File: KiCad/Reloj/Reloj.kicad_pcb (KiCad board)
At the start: 2 copper layers, 69.5 x 69.5 mm, 37 parts, among them J1 SOCKET_UP, J12 PLACA, J13 Conn_01x08_SocketMPU, J14 Conn_01x04_Socket, J15 Screw_Terminal_01x02, J16 Conn_01x02, J17 Conn_01x06_Socket, J18 Conn_01x02, J19 Conn_01x03, J21 Conn_01x02, J4 PLACA, J7 HEADER_DOWN, J8 PLACA, SW1 SW_SPDT, U1 25CSM04xxSN

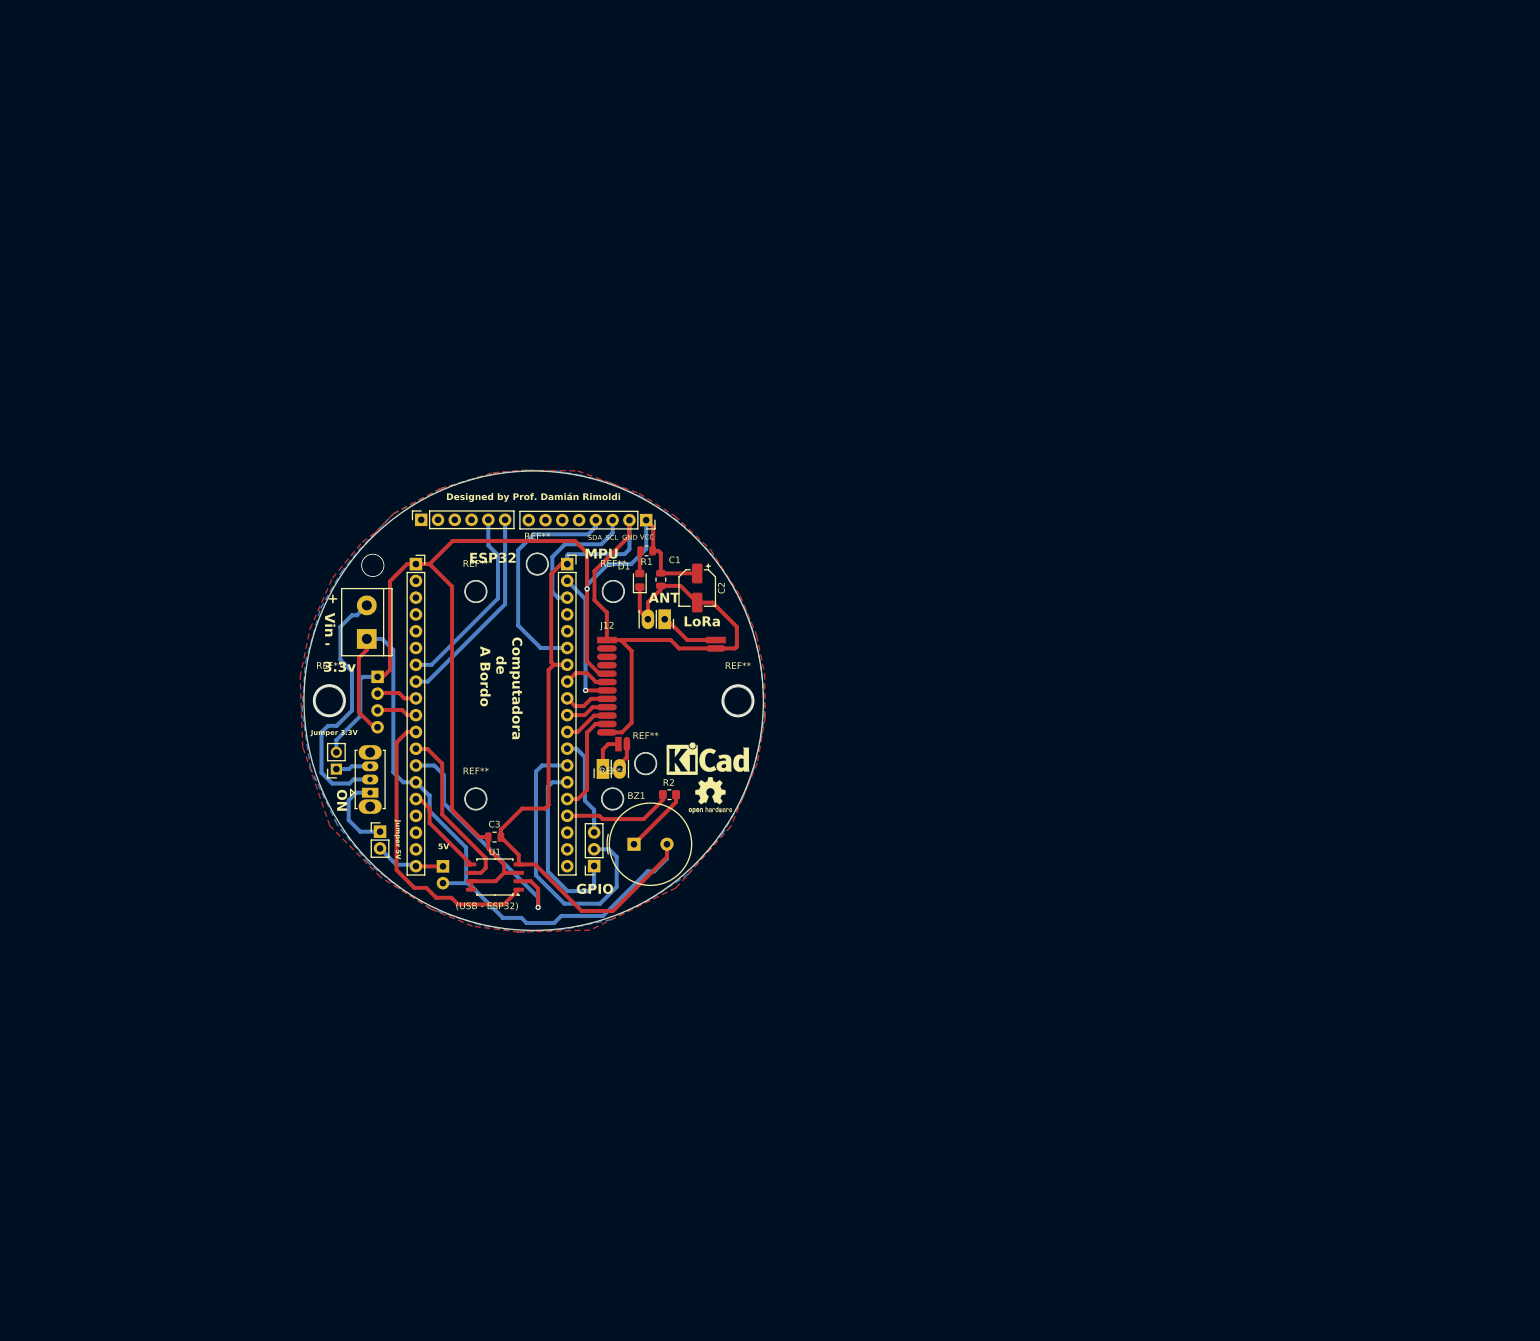
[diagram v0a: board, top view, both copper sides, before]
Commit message: Selecciono footprints y disposicion prelimar de PCB
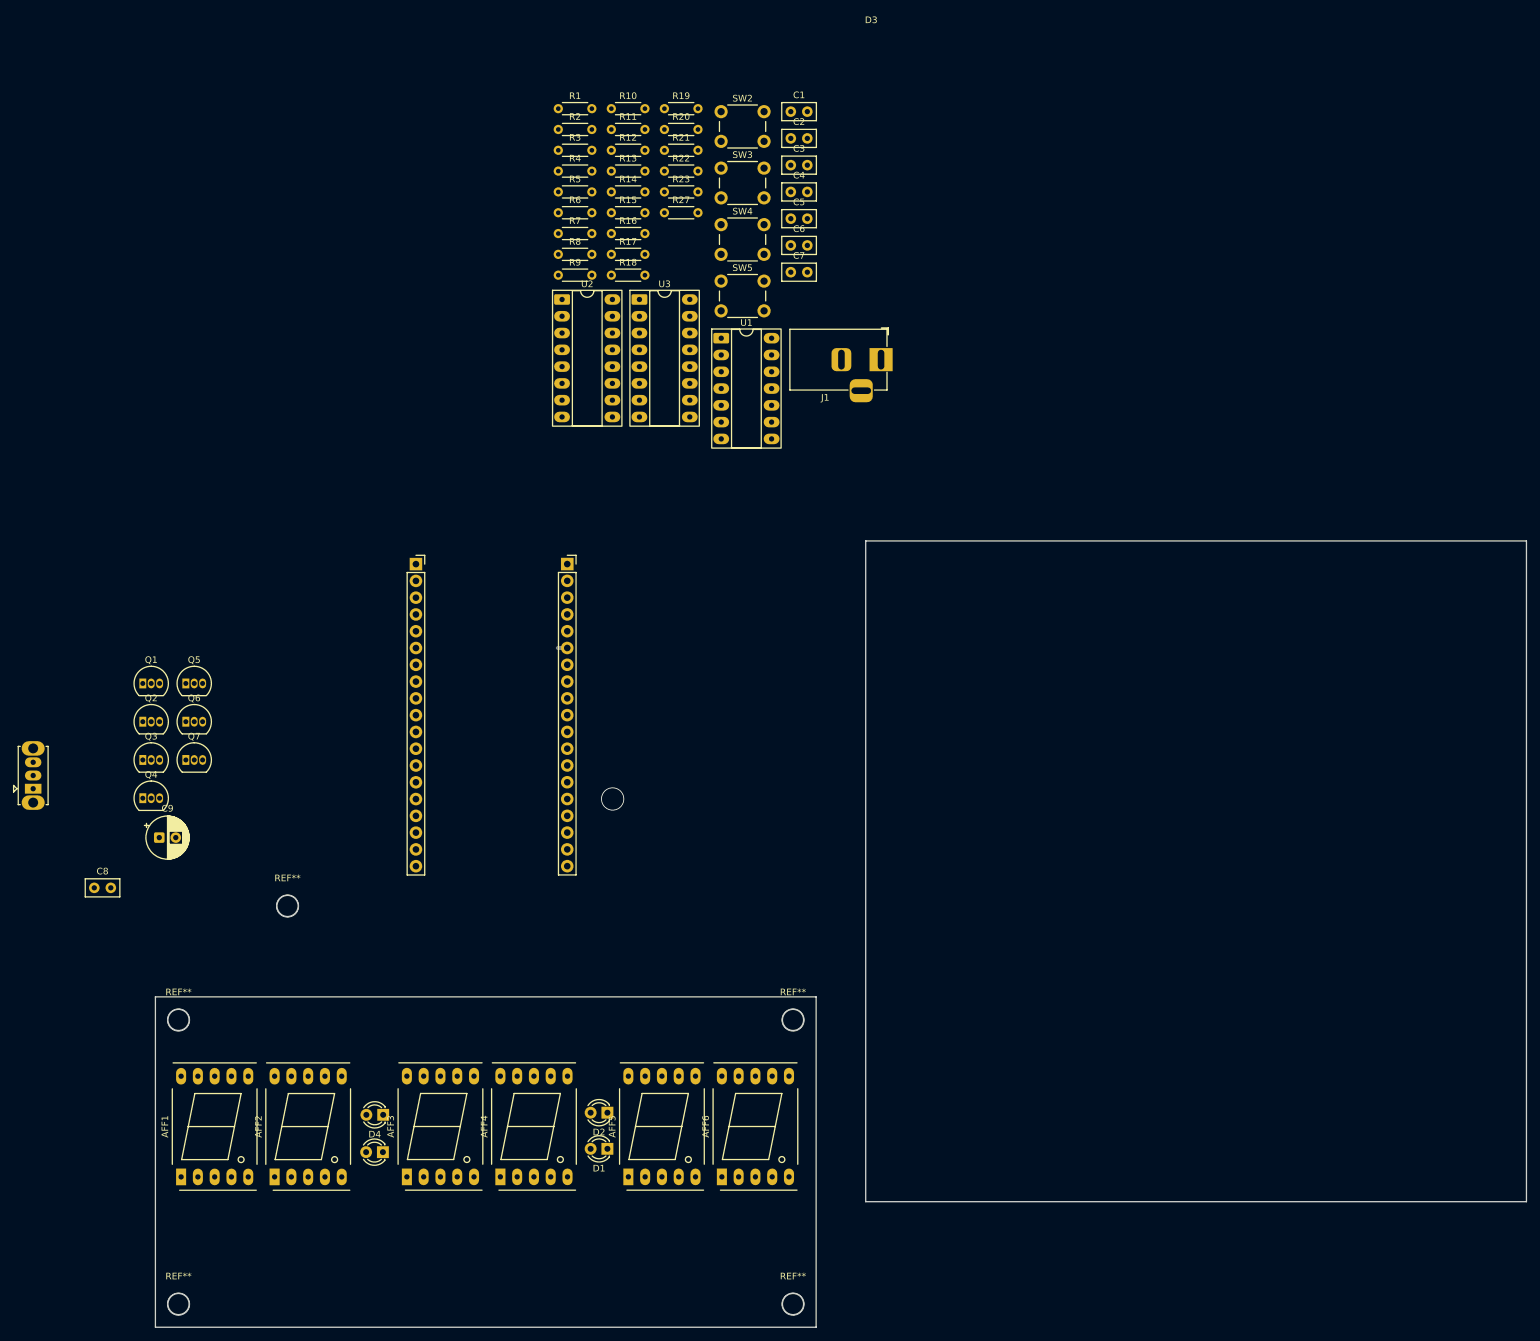
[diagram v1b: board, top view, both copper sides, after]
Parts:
- removed BZ1: Buzzer, Buzzer_Beeper:Buzzer_TDK_PS1240P02BT_D12.2mm_H6.5mm
- removed G***: LOGO, Imagenes:Cohete2
- removed G***: LOGO, Imagenes:CDRSys2Chico
- removed J12: PLACA, Connector_PinHeader_1.27mm:PinHeader_1x12_P1.27mm_Vertical
- removed J13: Conn_01x08_SocketMPU, Connector_PinSocket_2.54mm:PinSocket_1x08_P2.54mm_Vertical
- removed J14: Conn_01x04_Socket, Connector_PinSocket_2.54mm:PinSocket_1x04_P2.54mm_Vertical
- removed J15: Screw_Terminal_01x02, TerminalBlock:TerminalBlock_bornier-2_P5.08mm
- removed J16, J21: Conn_01x02, Connector_PinSocket_2.54mm:PinSocket_1x02_P2.54mm_Vertical
- removed J17: Conn_01x06_Socket, Connector_PinSocket_2.54mm:PinSocket_1x06_P2.54mm_Vertical
- removed J18: Conn_01x02, Connector_PinHeader_2.54mm:PinHeader_1x02_P2.54mm_Vertical
- removed J19: Conn_01x03, Connector_PinSocket_2.54mm:PinSocket_1x03_P2.54mm_Vertical
- removed J4, J8: PLACA, Connector_PinHeader_1.27mm:PinHeader_1x02_P1.27mm_Vertical
- removed J7: HEADER_DOWN, Connector_PinHeader_2.54mm:PinHeader_1x02_P2.54mm_Vertical
- removed the REF** at (112.2, 55.7)
- removed the REF** at (108.0, 70.0)
- removed the REF** at (104.3, 69.9)
- removed the REF** at (72.5, 39.1)
- removed the REF** at (107.6, 65.0)
- removed the REF** at (81.8, 35.0)
- removed the REF** at (98.2, 65.2)
- removed the REF** at (50.3, 55.7)
- removed the REF** at (93.3, 39.1)
- removed the REF** at (93.2, 70.5)
- added AFF1: LTS-6980HR, Display_7Segment:7SegmentLED_LTS6760_LTS6780, F.Cu at (27.9, 127.8)
- added AFF2: LTS-6980HR, Display_7Segment:7SegmentLED_LTS6760_LTS6780, F.Cu at (42.0, 127.8)
- added AFF3: LTS-6980HR, Display_7Segment:7SegmentLED_LTS6760_LTS6780, F.Cu at (62.1, 127.7)
- added AFF4: LTS-6980HR, Display_7Segment:7SegmentLED_LTS6760_LTS6780, F.Cu at (76.2, 127.7)
- added AFF5: LTS-6980HR, Display_7Segment:7SegmentLED_LTS6760_LTS6780, F.Cu at (95.6, 127.7)
- added AFF6: LTS-6980HR, Display_7Segment:7SegmentLED_LTS6760_LTS6780, F.Cu at (109.7, 127.7)
- added C4: 0.1uF, Capacitor_THT:C_Disc_D5.0mm_W2.5mm_P2.50mm, F.Cu at (120.2, -21.3)
- added C5: 0.1uF, Capacitor_THT:C_Disc_D5.0mm_W2.5mm_P2.50mm, F.Cu at (120.2, -17.3)
- added C6: 0.1uF, Capacitor_THT:C_Disc_D5.0mm_W2.5mm_P2.50mm, F.Cu at (120.2, -13.2)
- added C7: 0.1uF, Capacitor_THT:C_Disc_D5.0mm_W2.5mm_P2.50mm, F.Cu at (120.2, -9.18)
- added C8: 0.1uF, Capacitor_THT:C_Disc_D5.0mm_W2.5mm_P2.50mm, F.Cu at (14.8, 84.0)
- added C9: 100uF 16V, Capacitor_THT:CP_Radial_D6.3mm_P2.50mm, F.Cu at (24.6, 76.4)
- added D2: LED, LED_THT:LED_D3.0mm, F.Cu at (92.4, 118.0)
- added D3: LED, LED_THT:LED_D3.0mm, F.Cu at (58.4, 124.0)
- added D4: LED, LED_THT:LED_D3.0mm, F.Cu at (58.5, 118.4)
- added Q1: BC548, Package_TO_SOT_THT:TO-92_Inline, F.Cu at (22.1, 53.1)
- added Q2: BC548, Package_TO_SOT_THT:TO-92_Inline, F.Cu at (22.1, 58.9)
- added Q3: BC548, Package_TO_SOT_THT:TO-92_Inline, F.Cu at (22.1, 64.6)
- added Q4: BC548, Package_TO_SOT_THT:TO-92_Inline, F.Cu at (22.1, 70.4)
- added Q5: BC548, Package_TO_SOT_THT:TO-92_Inline, F.Cu at (28.6, 53.1)
- added Q6: BC548, Package_TO_SOT_THT:TO-92_Inline, F.Cu at (28.6, 58.9)
- added Q7: BC548, Package_TO_SOT_THT:TO-92_Inline, F.Cu at (28.6, 64.6)
- added R10: 4.7k, Resistor_THT:R_Axial_DIN0204_L3.6mm_D1.6mm_P5.08mm_Horizontal, F.Cu at (93.0, -33.9)
- added R11: 4.7k, Resistor_THT:R_Axial_DIN0204_L3.6mm_D1.6mm_P5.08mm_Horizontal, F.Cu at (93.0, -30.8)
- added R12: 4.7k, Resistor_THT:R_Axial_DIN0204_L3.6mm_D1.6mm_P5.08mm_Horizontal, F.Cu at (93.0, -27.6)
- added R13: 4.7k, Resistor_THT:R_Axial_DIN0204_L3.6mm_D1.6mm_P5.08mm_Horizontal, F.Cu at (93.0, -24.5)
- added R14: 4.7k, Resistor_THT:R_Axial_DIN0204_L3.6mm_D1.6mm_P5.08mm_Horizontal, F.Cu at (93.0, -21.3)
- added R15: 100, Resistor_THT:R_Axial_DIN0204_L3.6mm_D1.6mm_P5.08mm_Horizontal, F.Cu at (93.0, -18.2)
- added R16: 100, Resistor_THT:R_Axial_DIN0204_L3.6mm_D1.6mm_P5.08mm_Horizontal, F.Cu at (93.0, -15.0)
- added R17: 330, Resistor_THT:R_Axial_DIN0204_L3.6mm_D1.6mm_P5.08mm_Horizontal, F.Cu at (93.0, -11.9)
- added R18: 330, Resistor_THT:R_Axial_DIN0204_L3.6mm_D1.6mm_P5.08mm_Horizontal, F.Cu at (93.0, -8.72)
- added R19: 330, Resistor_THT:R_Axial_DIN0204_L3.6mm_D1.6mm_P5.08mm_Horizontal, F.Cu at (101.0, -33.9)
- added R20: 330, Resistor_THT:R_Axial_DIN0204_L3.6mm_D1.6mm_P5.08mm_Horizontal, F.Cu at (101.0, -30.8)
- added R21: 330, Resistor_THT:R_Axial_DIN0204_L3.6mm_D1.6mm_P5.08mm_Horizontal, F.Cu at (101.0, -27.6)
- added R22: 330, Resistor_THT:R_Axial_DIN0204_L3.6mm_D1.6mm_P5.08mm_Horizontal, F.Cu at (101.0, -24.5)
- added R23: 330, Resistor_THT:R_Axial_DIN0204_L3.6mm_D1.6mm_P5.08mm_Horizontal, F.Cu at (101.0, -21.3)
- added R27: 4.7k, Resistor_THT:R_Axial_DIN0204_L3.6mm_D1.6mm_P5.08mm_Horizontal, F.Cu at (101.0, -18.2)
- added R3: 10K, Resistor_THT:R_Axial_DIN0204_L3.6mm_D1.6mm_P5.08mm_Horizontal, F.Cu at (85.0, -27.6)
- added R4: 100, Resistor_THT:R_Axial_DIN0204_L3.6mm_D1.6mm_P5.08mm_Horizontal, F.Cu at (85.0, -24.5)
- added R5: 10K, Resistor_THT:R_Axial_DIN0204_L3.6mm_D1.6mm_P5.08mm_Horizontal, F.Cu at (85.0, -21.3)
- added R6: 100, Resistor_THT:R_Axial_DIN0204_L3.6mm_D1.6mm_P5.08mm_Horizontal, F.Cu at (85.0, -18.2)
- added R7: 10K, Resistor_THT:R_Axial_DIN0204_L3.6mm_D1.6mm_P5.08mm_Horizontal, F.Cu at (85.0, -15.0)
- added R8: 100, Resistor_THT:R_Axial_DIN0204_L3.6mm_D1.6mm_P5.08mm_Horizontal, F.Cu at (85.0, -11.9)
- added R9: 4.7k, Resistor_THT:R_Axial_DIN0204_L3.6mm_D1.6mm_P5.08mm_Horizontal, F.Cu at (85.0, -8.72)
- added REF**: MountingHole_3.2mm_M3, MountingHole:MountingHole_3.2mm_M3, F.Cu at (27.5, 147.0)
- added REF**: MountingHole_3.2mm_M3, MountingHole:MountingHole_3.2mm_M3, F.Cu at (120.5, 147.0)
- added REF**: MountingHole_3.2mm_M3, MountingHole:MountingHole_3.2mm_M3, F.Cu at (27.5, 104.0)
- added REF**: MountingHole_3.2mm_M3, MountingHole:MountingHole_3.2mm_M3, F.Cu at (120.5, 104.0)
- added SW2: SW_Push, Button_Switch_THT:SW_PUSH_6mm_H4.3mm, F.Cu at (109.6, -33.5)
- added SW3: SW_Push, Button_Switch_THT:SW_PUSH_6mm_H4.3mm, F.Cu at (109.6, -24.9)
- added SW4: SW_Push, Button_Switch_THT:SW_PUSH_6mm_H4.3mm, F.Cu at (109.6, -16.4)
- added SW5: SW_Push, Button_Switch_THT:SW_PUSH_6mm_H4.3mm, F.Cu at (109.6, -7.83)
- added U2: 4050, Package_DIP:DIP-16_W7.62mm_Socket_LongPads, F.Cu at (85.5, -5.04)
- added U3: 74HC595, Package_DIP:DIP-16_W7.62mm_Socket_LongPads, F.Cu at (97.3, -5.04)
- C1: value 100nF -> 0.1uF; footprint Capacitor_SMD:C_0805_2012Metric -> Capacitor_THT:C_Disc_D5.0mm_W2.5mm_P2.50mm
- C2: value 100uF -> 0.1uF; footprint Capacitor_SMD:CP_Elec_5x3.9 -> Capacitor_THT:C_Disc_D5.0mm_W2.5mm_P2.50mm
- C3: value C_Polarized_Small -> 0.1uF; footprint Capacitor_SMD:C_0805_2012Metric -> Capacitor_THT:C_Disc_D5.0mm_W2.5mm_P2.50mm
- D1: footprint LED_SMD:LED_0805_2012Metric_Pad1.15x1.40mm_HandSolder -> LED_THT:LED_D3.0mm
- J1: value SOCKET_UP -> Jack-DC; footprint Connector_PinSocket_2.54mm:PinSocket_1x02_P2.54mm_Vertical -> Connector_BarrelJack:BarrelJack_Horizontal
- R1: value 1K -> 10K; footprint Resistor_SMD:R_0805_2012Metric -> Resistor_THT:R_Axial_DIN0204_L3.6mm_D1.6mm_P5.08mm_Horizontal
- R2: value R -> 100; footprint Resistor_SMD:R_0805_2012Metric_Pad1.20x1.40mm_HandSolder -> Resistor_THT:R_Axial_DIN0204_L3.6mm_D1.6mm_P5.08mm_Horizontal
- U1: value 25CSM04xxSN -> 74HC14; footprint Package_SO:SOIC-8_5.23x5.23mm_P1.27mm -> Package_DIP:DIP-14_W7.62mm_Socket_LongPads
- moved C3 111.1 mm to (120.2, -25.4)
- moved R2 102.1 mm to (85.0, -30.8), turned to 0 degrees
- moved U1 88.5 mm to (109.6, 0.81), turned to 0 degrees
- moved D1 86.2 mm to (92.4, 123.5), turned to 180 degrees
- moved C1 73.5 mm to (120.2, -33.5), turned to 0 degrees
- moved C2 69.5 mm to (120.2, -29.4), turned to 0 degrees
- moved R1 68.3 mm to (85.0, -33.9), turned to 0 degrees
- moved J1 51.1 mm to (133.8, 4.06), turned to 0 degrees
- moved SW1 51.0 mm to (5.50, 69.0)
- moved REF** 32.8 mm to (44.0, 86.7)
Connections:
- C1 pad 1: VCC -> Net-(C1-Pad1)
- C2 pad 1: VCC -> Net-(C2-Pad1)
- C3 pad 1: VCC -> Net-(C3-Pad1)
- D1 pad 1: GND -> Net-(D1-K)
- D1 pad 2: Net-(D1-A) -> 3,3V
- J1 pad 1: ANTENA -> GND
- J1 pad 2: GND -> 5v
- R1 pad 1: VCC -> 3,3V
- R1 pad 2: Net-(D1-A) -> Net-(R1-Pad2)
- R2 pad 1: Net-(BZ1-+) -> Net-(C1-Pad1)
- R2 pad 2: BUZZ -> Net-(R1-Pad2)
- U1 pad 1: HSS -> Net-(C1-Pad1)
- U1 pad 2: HMISO -> GPIO32
- U1 pad 3: VCC -> Net-(C2-Pad1)
- U1 pad 4: GND -> GPIO33
- U1 pad 5: HMOSI -> Net-(C3-Pad1)
- U1 pad 6: HCLK -> GPIO25
- U1 pad 7: VCC -> Net-(U1G-GND)
- U1 pad 8: VCC -> GPIO26
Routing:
- net GND: track 297.0 -> 0.17 mm
- net VCC: track 178.0 -> 0.00 mm, vias 1 -> 0
- net HSS: track 44.5 -> 0.00 mm
- net GPIO4: track 44.3 -> 0.00 mm
- net INVolt: track 39.1 -> 0.00 mm
- net HMISO: track 37.1 -> 0.02 mm, vias 1 -> 0
- net SDAMPU: track 35.6 -> 1.43 mm
- net GPIO33: track 31.1 -> 0.00 mm
- net GPIO32: track 29.1 -> 0.00 mm
- net GPIO0: track 27.7 -> 0.21 mm
- net HCLK: track 26.0 -> 0.08 mm
- net MOSI: track 21.0 -> 0.00 mm, vias 1 -> 0
- net SCLMPU: track 20.5 -> 0.00 mm
- net BUZZ: track 16.7 -> 0.00 mm
- net REST: track 15.8 -> 0.00 mm
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- removed copper zone on B.Cu, net GND
- removed copper zone on F.Cu, net GND
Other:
- board size 69.5 x 69.5 mm -> 207.5 x 119 mm
- board text removed: "(USB - ESP32)"
- board text removed: "+"
- board text removed: "-"
- board text removed: "3.3v"
- board text removed: "5V"
- board text removed: "ANT"
- board text removed: "CANSAT 2024"
- board text removed: "Computadora de A Bordo"
- board text removed: "Designed by Prof. Damián Rimoldi"
- board text removed: "ESP32"
- board text removed: "GND"
- board text removed: "GPIO"
- board text removed: "GPS"
- board text removed: "Jumper 3.3V"
- board text removed: "Jumper 5V"
- board text removed: "LoRa"
- board text removed: "MPU"
- board text removed: "ON"
- board text removed: "P0"
- board text removed: "P16"
- board text removed: "P32"
- board text removed: "P33"
- board text removed: "P34"
- board text removed: "P35"
- board text removed: "P36"
- board text removed: "P39"
- board text removed: "P4"
- board text removed: "Rev 1.0.0"
- board text removed: "Rx"
- board text removed: "SAGA I"
- board text removed: "SCL"
- board text removed: "SDA"
- board text removed: "Tx"
- board text removed: "UTN - EESTNº4"
- board text removed: "VCC"
- board text removed: "Vin"
- board text removed: "_"

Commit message: Agrego version 3 placas, distribucion principal y conectores
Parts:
- removed the REF** at (44.0, 86.7)
- added J2: Conn_2Rows-15Pins, Connector_IDC:IDC-Header_2x07_P2.54mm_Vertical, F.Cu at (95.8, 146.5)
- added J3: Conn_2Rows-11Pins, Connector_IDC:IDC-Header_2x05_P2.54mm_Vertical, F.Cu at (36.8, 146.5)
- added J4: Conn_2Rows-15Pins, Connector_IDC:IDC-Header_2x07_P2.54mm_Vertical, F.Cu at (213.9, 145.5)
- added J5: Conn_2Rows-11Pins, Connector_IDC:IDC-Header_2x05_P2.54mm_Vertical, F.Cu at (227.0, 104.2)
- added J6: Conn_2Rows-11Pins, Connector_IDC:IDC-Header_2x05_P2.54mm_Vertical, F.Cu at (171.0, 79.8)
- added J7: Conn_2Rows-11Pins, Connector_IDC:IDC-Header_2x05_P2.54mm_Vertical, F.Cu at (171.0, 69.5)
- added J8: Conn_2Rows-15Pins, Connector_IDC:IDC-Header_2x07_P2.54mm_Vertical, F.Cu at (227.9, 79.8)
- added J9: Conn_2Rows-15Pins, Connector_IDC:IDC-Header_2x07_P2.54mm_Vertical, F.Cu at (227.9, 69.5)
- added REF**: MountingHole_3.2mm_M3, MountingHole:MountingHole_3.2mm_M3, F.Cu at (253.2, 80.0)
- added REF**: MountingHole_3.2mm_M3, MountingHole:MountingHole_3.2mm_M3, F.Cu at (160.8, 37.5)
- added REF**: MountingHole_3.2mm_M3, MountingHole:MountingHole_3.2mm_M3, F.Cu at (248.0, 146.2)
- added REF**: MountingHole_3.2mm_M3, MountingHole:MountingHole_3.2mm_M3, F.Cu at (155.5, 146.2)
- added REF**: MountingHole_3.2mm_M3, MountingHole:MountingHole_3.2mm_M3, F.Cu at (248.0, 103.8)
- added REF**: MountingHole_3.2mm_M3, MountingHole:MountingHole_3.2mm_M3, F.Cu at (253.2, 37.5)
- added REF**: MountingHole_3.2mm_M3, MountingHole:MountingHole_3.2mm_M3, F.Cu at (155.5, 103.8)
- added REF**: MountingHole_3.2mm_M3, MountingHole:MountingHole_3.2mm_M3, F.Cu at (160.8, 80.0)
- moved SW1 250.8 mm to (247.0, 136.6)
- moved C8 212.4 mm to (222.4, 128.6)
- moved C9 212.4 mm to (232.2, 121.0)
- moved SW2 181.6 mm to (55.8, 140.0), turned to 90 degrees
- moved SW3 170.9 mm to (65.0, 140.0), turned to 90 degrees
- moved SW4 160.3 mm to (74.2, 140.0), turned to 90 degrees
- moved J1 158.0 mm to (241.5, 119.7), turned to 180 degrees
- moved SW5 150.2 mm to (83.2, 140.0), turned to 90 degrees
- moved esp1 137.5 mm to (156.4, 136.4), turned to 90 degrees
- moved U1 125.2 mm to (228.5, 40.0)
- moved C5 123.4 mm to (231.2, 36.5)
- moved U3 115.1 mm to (203.2, 39.8)
- moved esp32_1 105.2 mm to (156.3, 113.5), turned to 90 degrees
- moved U2 103.5 mm to (178.9, 39.7)
- moved Q1 102.2 mm to (124.2, 50.2)
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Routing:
- net HMOSI: track 0.63 -> 0.00 mm
- net (no net): vias 6 -> 13
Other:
- board size 207.5 x 119 mm -> 233 x 116.8 mm
